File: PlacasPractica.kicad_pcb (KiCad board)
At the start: 2 copper layers, 65 parts, among them J1 USB_OTG, J2 Conn_01x10, J3 Conn_01x10, J4 CONN_02X05, SW1 SW_Push, U1 SAMD20J18A-AU, U2 XBEE, U4 XC6220B331MR-G, U5 XC6220B331MR-G, U6 XC6220B331MR-G, Y1 Crystal

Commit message: Inicio diseño PCB
Se ha iniciado con el diseño de la PCB
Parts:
- added U3: MB85RC64VPNF-G-JNERE1, Housings_SOIC:SOIC-8_3.9x4.9mm_Pitch1.27mm, F.Cu at (142.6, 103.0)
- JP2, JP3, JP4, JP5: moved to B.Cu
- moved C15 194.8 mm to (251.1, 33.4), turned to 270 degrees
- moved JP8 192.9 mm to (240.4, 103.4), turned to 90 degrees
- moved R1 192.2 mm to (79.1, 175.4), turned to 180 degrees
- moved U6 173.1 mm to (247.0, 101.6), turned to 270 degrees
- moved C17 167.6 mm to (253.4, 103.4), turned to 270 degrees
- moved D6 158.7 mm to (242.6, 98.6), turned to 90 degrees
- moved D7 158.7 mm to (228.1, 40.8)
- moved C13 153.8 mm to (247.1, 98.6)
- moved JP6 149.2 mm to (237.3, 32.9)
- moved U2 147.8 mm to (156.8, 92.3), turned to 270 degrees
- moved R11 147.1 mm to (245.7, 104.6)
- moved C16 134.6 mm to (243.9, 62.3), turned to 270 degrees
- moved C5 126.1 mm to (121.3, 110.6), turned to 180 degrees
- moved R10 124.1 mm to (236.2, 63.5)
- moved R3 116.0 mm to (148.3, 101.3), turned to 270 degrees
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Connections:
- C1 pad 2: +3V3 -> /3V3
- C2 pad 2: +3V3 -> /3V3
- C3 pad 2: +3V3 -> /3V3
- C4 pad 2: +3V3 -> /3V3
- L1 pad 1: +3V3 -> /3V3
- U1 pad 21: +3V3 -> /3V3
- U1 pad 34: +3V3 -> /3V3
- U1 pad 48: +3V3 -> /3V3
- U1 pad 56: +3V3 -> /3V3
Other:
- net class Alimentacion added: clearance 0.2, trace_width 0.7, via_dia 0.6, via_drill 0.4
- net class Default: trace_width 0.25 -> 0.5

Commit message: Diseño pcb, punto intermedio.
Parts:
- C1, C10, C12, C13, C14, C2, C3, C4, C8, C9, D2, D3, D4, D5, D6, JP1, JP6, JP7, JP8, R1, R10, R11, R2, R3, R4, R5, R6, R7, R8, R9, U4, U5, U6: moved to B.Cu
- moved C15 169.7 mm to (93.1, 95.5), turned to 180 degrees
- moved D4 169.0 mm to (88.7, 102.8), turned to 180 degrees
- moved U4 165.6 mm to (95.0, 101.8), turned to 90 degrees
- moved C14 162.3 mm to (95.0, 98.9), turned to 180 degrees
- moved C17 161.5 mm to (93.0, 121.9), turned to 180 degrees
- moved C13 160.6 mm to (88.7, 125.3), turned to 180 degrees
- moved C12 158.6 mm to (88.7, 112.9), turned to 180 degrees
- moved C16 158.1 mm to (93.0, 109.2), turned to 180 degrees
- moved D6 156.7 mm to (88.7, 127.8), turned to 180 degrees
- moved D5 155.4 mm to (88.7, 115.3), turned to 180 degrees
- moved U6 155.0 mm to (94.1, 126.9), turned to 90 degrees
- moved R9 154.5 mm to (91.3, 95.8)
- moved JP6 154.3 mm to (96.4, 95.9), turned to 270 degrees
- moved U5 153.2 mm to (94.1, 114.4), turned to 90 degrees
- moved R11 152.6 mm to (94.3, 123.5)
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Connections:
- 0.1uF1 pad 1: Net-(0.1uF1-Pad1) -> /3V3
- J1 pad 1: /5v -> +5V
- U3 pad 8: Net-(0.1uF1-Pad1) -> /3V3
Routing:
- net /3V3_SENS: track 0.00 -> 186.8 mm, vias 0 -> 1
- net /3V3_COM: track 0.05 -> 121.1 mm, vias 0 -> 1
- net /3V3: track 0.00 -> 105.3 mm, vias 0 -> 4
- net /D11: track 0.00 -> 55.6 mm, vias 0 -> 1
- net /VCC_COM: track 0.00 -> 53.1 mm, vias 0 -> 5
- net /TXD: track 0.00 -> 52.4 mm, vias 0 -> 2
- net /RTS: track 0.00 -> 51.1 mm, vias 0 -> 2
- net /SDA: track 0.00 -> 51.1 mm, vias 0 -> 1
- net +5V: track 0.00 -> 51.0 mm, vias 0 -> 1
- net /SCL: track 0.00 -> 49.7 mm, vias 0 -> 1
- net /RXD: track 0.00 -> 49.4 mm, vias 0 -> 1
- net /D5: track 0.00 -> 45.4 mm, vias 0 -> 2
- net /D6: track 0.00 -> 45.2 mm, vias 0 -> 1
- net /D3: track 0.00 -> 44.7 mm, vias 0 -> 1
- net /VCC_SENS: track 0.00 -> 42.0 mm, vias 0 -> 1
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- added copper zone on B.Cu, net GND
- added copper zone on F.Cu, net GND
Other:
- net class Alimentacion: trace_width 0.7 -> 0.45
- net class Default: trace_width 0.5 -> 0.25

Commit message: Pistas finalizadas.
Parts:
- moved 4k2 5.11 mm to (136.6, 99.2), turned to 90 degrees
- moved J2 4.63 mm to (133.3, 127.5)
- moved DIGITAL2 3.76 mm to (153.2, 125.5)
- moved DIGITAL1 3.51 mm to (141.5, 125.5)
- moved 0.1uF1 3.12 mm to (141.9, 103.7)
- moved U3 2.29 mm to (142.6, 98.7)
- moved 4k1 1.04 mm to (133.7, 99.2), turned to 90 degrees
- moved J3 0.59 mm to (113.0, 79.2)
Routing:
- net /3V3: track 105.3 -> 219.1 mm, vias 4 -> 8
- net /A1: track 0.00 -> 63.4 mm, vias 0 -> 2
- net GND: track 4.97 -> 66.9 mm, vias 1 -> 7
- net /A0: track 0.00 -> 59.3 mm, vias 0 -> 2
- net /SCK: track 0.00 -> 43.0 mm, vias 0 -> 2
- net /3V3_COM: track 121.1 -> 155.0 mm
- net Net-(JP3-Pad2): track 0.00 -> 30.9 mm, vias 0 -> 1
- net /RI_AS: track 0.00 -> 25.3 mm, vias 0 -> 3
- net /SDA: track 51.1 -> 69.9 mm, vias 1 -> 2
- net Net-(JP2-Pad2): track 0.00 -> 18.4 mm, vias 0 -> 3
- net /VCC_SENS: track 42.0 -> 54.2 mm
- net /D11: track 55.6 -> 64.7 mm, vias 1 -> 0
- net /VCC_COM: track 53.1 -> 61.1 mm
- net Net-(R3-Pad1): track 20.2 -> 25.7 mm
- net /D4: track 30.0 -> 34.5 mm
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
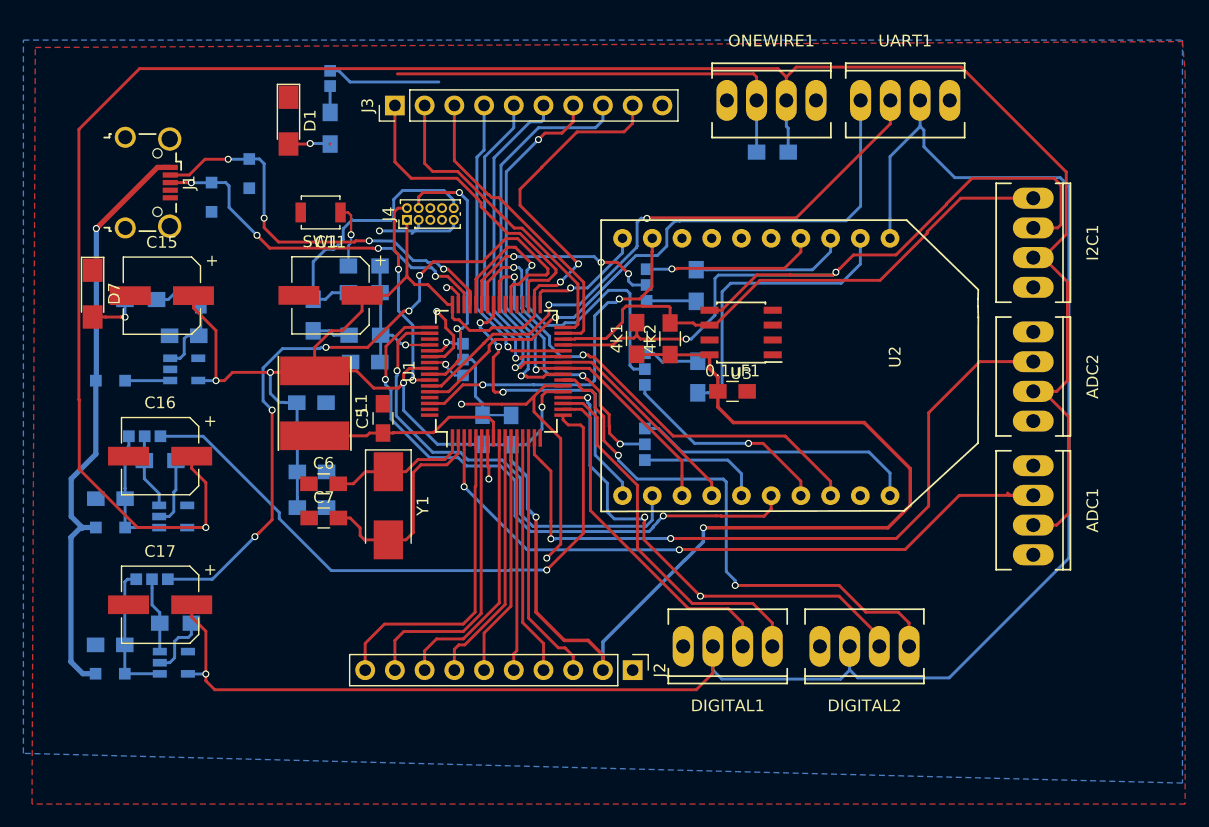
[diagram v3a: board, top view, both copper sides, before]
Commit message: Agujeros de montaje y seriagrafía añadidos
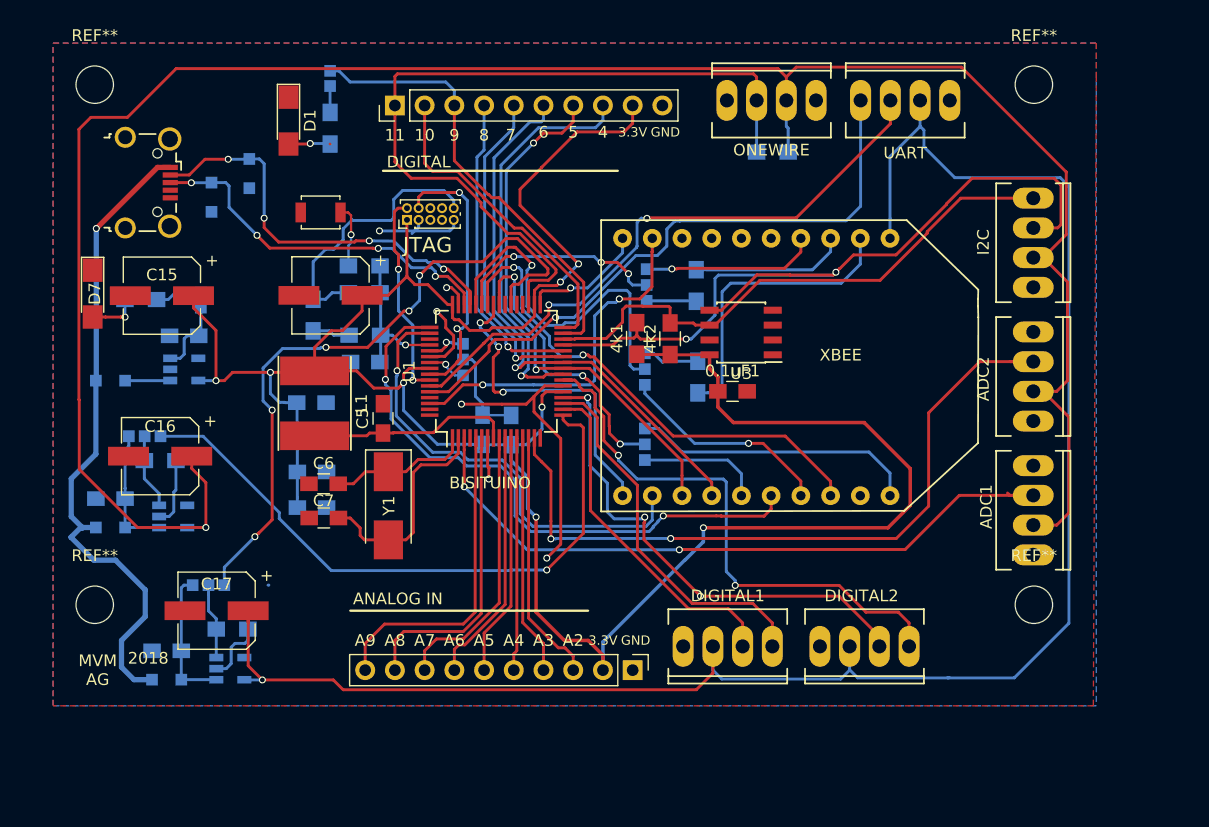
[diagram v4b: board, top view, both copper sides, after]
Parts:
- added REF**: MountingHole_3.2mm_M3, Mounting_Holes:MountingHole_3.2mm_M3, F.Cu at (87.4, 121.9)
- added REF**: MountingHole_3.2mm_M3, Mounting_Holes:MountingHole_3.2mm_M3, F.Cu at (87.4, 77.5)
- added REF**: MountingHole_3.2mm_M3, Mounting_Holes:MountingHole_3.2mm_M3, F.Cu at (167.6, 77.5)
- added REF**: MountingHole_3.2mm_M3, Mounting_Holes:MountingHole_3.2mm_M3, F.Cu at (167.6, 121.9)
- C1, C2, C3, C4: value C -> 10uF
- C5: value C -> 100nF
- JP2: value JUMPER3 -> JxBEE_TXD
- JP3: value JUMPER3 -> J_xBEE_RXD
- JP5: value Jumper_NC_Dual -> J_vddcD21_vddcL21
- JP7: value Jumper_NC_Dual -> J_Vsensor_Vcc
- JP8: value Jumper_NC_Dual -> J_Vcom_Vcc
- moved C13 4.85 mm to (93.5, 125.9)
- moved C17 4.85 mm to (97.8, 122.4)
- moved D6 4.85 mm to (93.5, 128.3)
- moved U6 4.85 mm to (99.0, 127.4)
- moved JP8 4.85 mm to (97.1, 120.2)
- moved R11 4.85 mm to (99.1, 124.0)
- renumbered I2C1 to I2C, ONEWIRE1 to ONEWIRE, UART1 to UART
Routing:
- net +5V: track 51.0 -> 56.6 mm
- net /VCC_COM: track 61.1 -> 57.4 mm
- net /D9: track 35.8 -> 38.7 mm
- net /D11: track 64.7 -> 67.5 mm
- net /3V3_COM: track 155.0 -> 154.1 mm
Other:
- board text added: "10"
- board text added: "11"
- board text added: "2018"
- board text added: "3.3V"
- board text added: "4"
- board text added: "5"
- board text added: "6"
- board text added: "7"
- board text added: "8"
- board text added: "9"
- board text added: "A2"
- board text added: "A3"
- board text added: "A4"
- board text added: "A5"
- board text added: "A6"
- board text added: "A7"
- board text added: "A8"
- board text added: "A9"
- board text added: "ANALOG IN"
- board text added: "BISITUINO"
- board text added: "DIGITAL"
- board text added: "GND"
- board text added: "JTAG"
- board text added: "MVM AG"
- board text added: "XBEE"

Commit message: Placa finalizada.
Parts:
- added G***: LOGO, Logos:LOGO_bisite_grande, F.Cu at (161.8, 123.4)
- moved REF** 2.54 mm to (87.4, 124.5)
- moved REF** 2.54 mm to (167.6, 124.5)
- renumbered JP4 to Ri
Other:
- board text added: "3.3"
- board text added: "A0"
- board text added: "A1"
- board text added: "ASSOC"
- board text added: "D0"
- board text added: "D1"
- board text added: "D11"
- board text added: "D2"
- board text added: "D21"
- board text added: "D3"
- board text added: "L21"
- board text added: "LED"
- board text added: "NC"
- board text added: "RESET"
- board text added: "RXD"
- board text added: "SCL"
- board text added: "SDA"
- board text added: "TXD"
- board text added: "VccCom"
- board text added: "VccSens"
- board text added: "XBMISO"
- board text added: "XBRX"
- board text added: "XBSS"
- board text added: "XBTX"
